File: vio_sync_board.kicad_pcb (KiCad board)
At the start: 2 copper layers, 50 x 57 mm, 12 parts, among them J1 Conn_IMU_Pi_Cam, Q1 BSS138, U1 MCP1700x-180xxTT

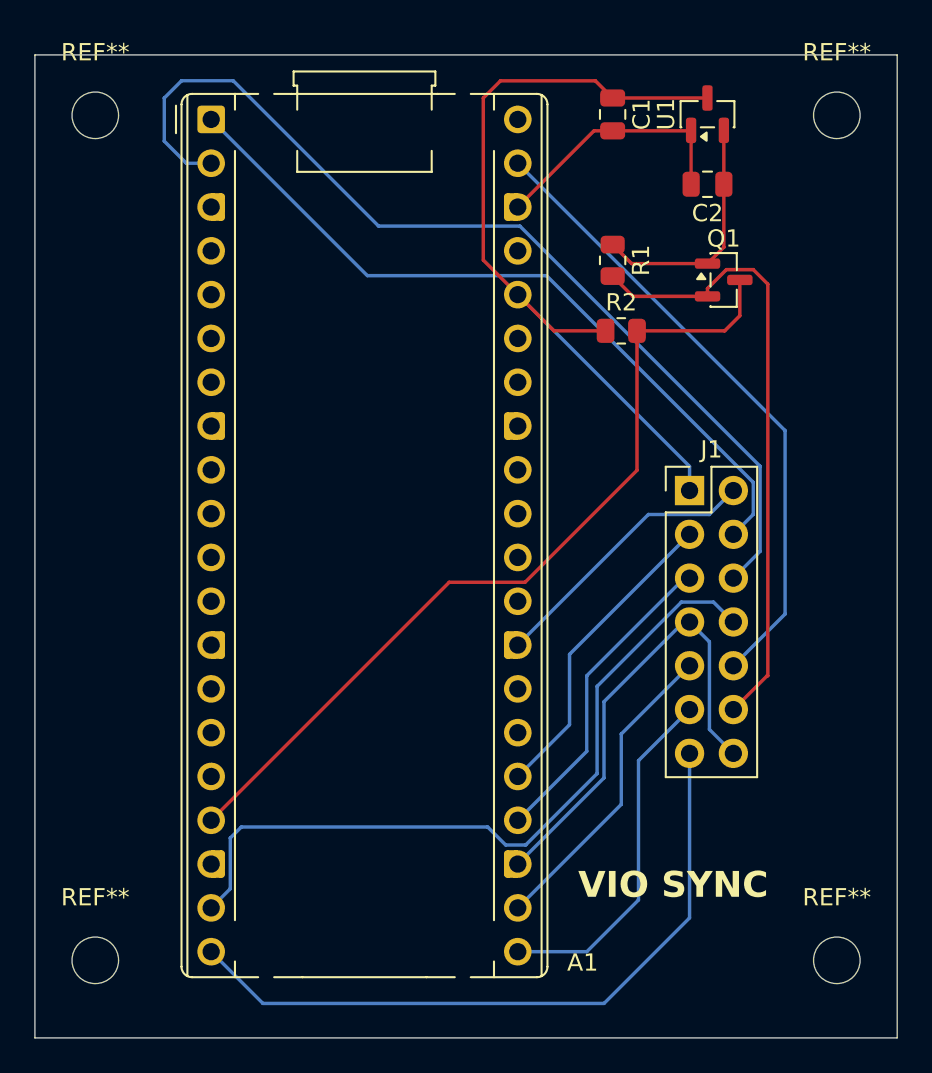
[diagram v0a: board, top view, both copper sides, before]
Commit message: refine header and hole position
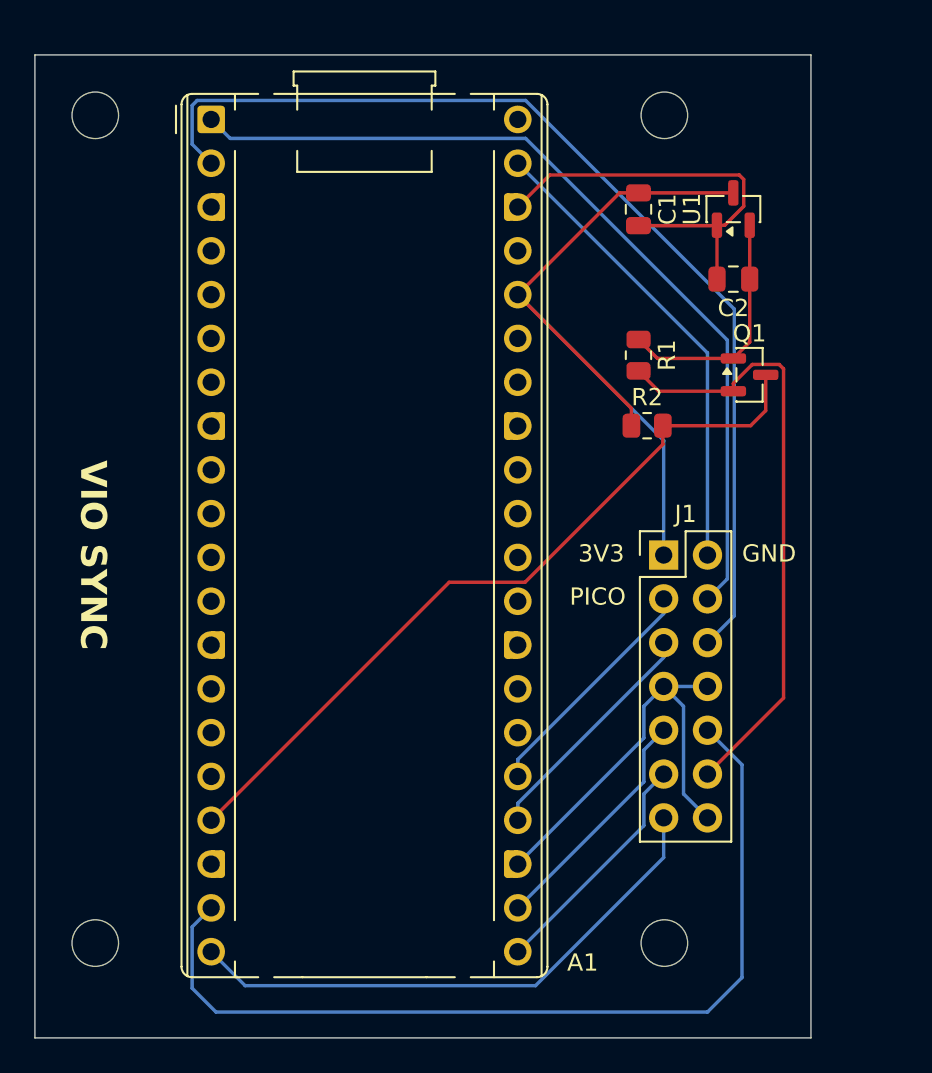
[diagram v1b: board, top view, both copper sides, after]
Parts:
- moved REF** 10.0 mm to (77.0, 98.0)
- moved REF** 10.0 mm to (77.0, 50.0)
- moved C1 5.70 mm to (75.5, 55.5)
- moved C2 5.70 mm to (81.0, 59.5)
- moved Q1 5.70 mm to (81.9, 65.0)
- moved R1 5.70 mm to (75.5, 63.9)
- moved R2 5.70 mm to (76.0, 68.0)
- moved U1 5.70 mm to (81.0, 55.4)
- moved J1 4.03 mm to (77.0, 75.5)
- moved REF** 1.00 mm to (44.0, 98.0)
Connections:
- J1 pad 10: /VSYS -> /TSYNC
- J1 pad 2: /GND -> /VSYS
- J1 pad 8: /TSYNC -> /GND
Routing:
- net /TSYNC: track 43.7 -> 53.6 mm
- net /VSYS: track 36.8 -> 27.3 mm
- net /IMU_INT: track 40.6 -> 32.4 mm
- net /GND: track 58.3 -> 50.2 mm
- net /UART0_TX: track 43.6 -> 50.7 mm
- net /SPI0_POCI: track 20.5 -> 13.8 mm
- net /SPI0_PICO: track 18.7 -> 13.8 mm
- net /XTR_3V3: track 49.6 -> 44.7 mm
- net /SPI0_SCK: track 18.3 -> 13.8 mm
- net /SPI0_CS: track 18.2 -> 13.8 mm
- net /3V3: track 47.5 -> 43.9 mm
- net /UART0_RX: track 57.1 -> 60.4 mm
- net /XTR_1V8: track 36.3 -> 35.2 mm
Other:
- board size 50 x 57 mm -> 45 x 57 mm
- board text added: "3V3"
- board text added: "GND"
- board text added: "PICO"

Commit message: track width
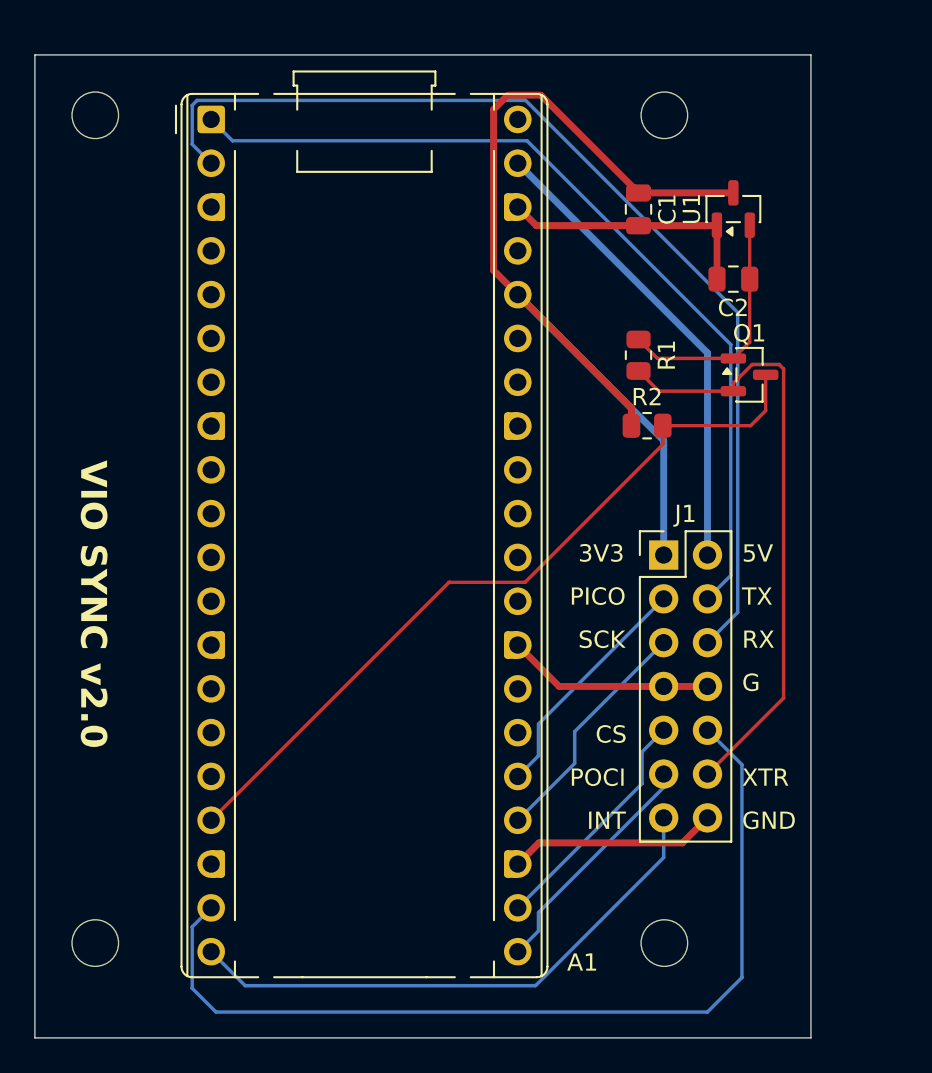
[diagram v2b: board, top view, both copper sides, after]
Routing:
- net /3V3: track 43.9 -> 56.8 mm
- net /GND: track 50.2 -> 39.2 mm
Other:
- board text added: "5V"
- board text added: "CS"
- board text added: "G"
- board text added: "INT"
- board text added: "POCI"
- board text added: "RX"
- board text added: "SCK"
- board text added: "TX"
- board text added: "VIO SYNC v2.0"
- board text added: "XTR"
- board text removed: "VIO SYNC"

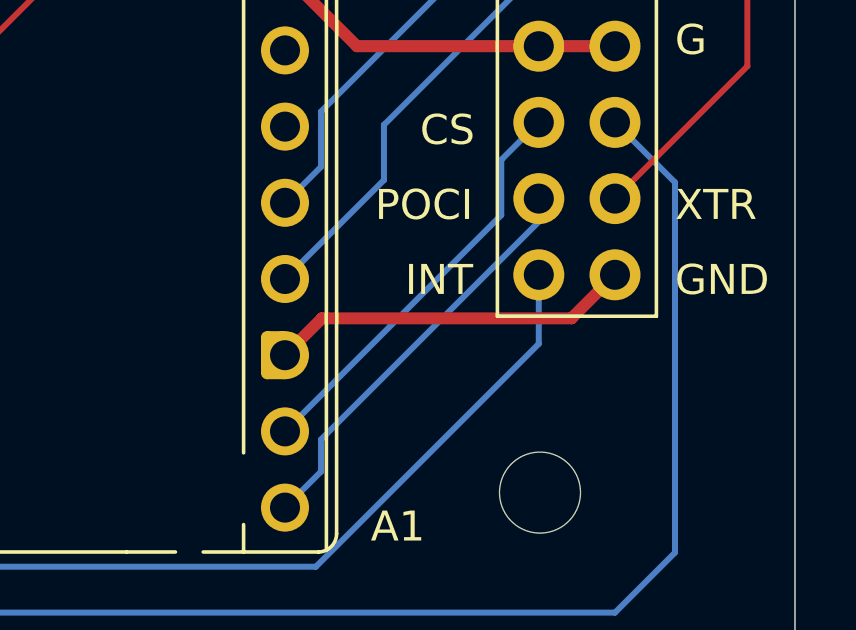
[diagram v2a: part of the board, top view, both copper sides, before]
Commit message: DNP pico & header
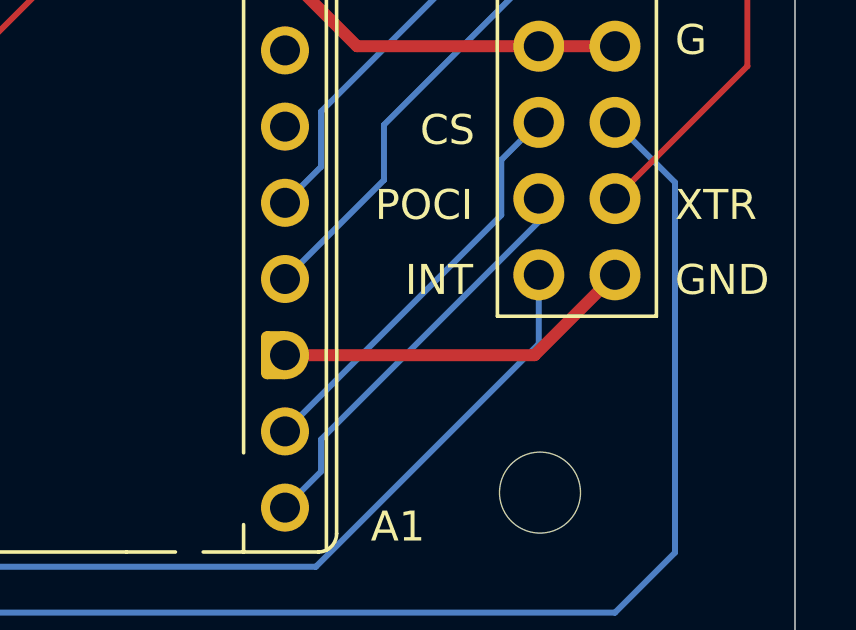
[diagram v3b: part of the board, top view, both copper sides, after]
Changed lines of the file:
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@@
 		(sheetname "/")
 		(sheetfile "vio_sync_board.kicad_sch")
-		(attr through_hole)
+		(attr through_hole exclude_from_bom dnp)
 		(fp_line
 			(start -1.38 -1.38)
@@
 		(sheetname "/")
 		(sheetfile "vio_sync_board.kicad_sch")
-		(attr through_hole)
+		(attr through_hole exclude_from_bom dnp)
 		(fp_line
 			(start -2.04 0.8)
@@
 	)
 	(segment
-		(start 78.049 92.191)
-		(end 69.729 92.191)
+		(start 76.82 93.42)
+		(end 68.5 93.42)
 		(width 0.4)
 		(layer "F.Cu")
@@
 	)
 	(segment
-		(start 75.5 56.4)
-		(end 69.58 56.4)
-		(width 0.4)
-		(layer "F.Cu")
-		(net 3)
-	)
-	(segment
-		(start 69.729 92.191)
-		(end 68.5 93.42)
+		(start 79.5 90.74)
+		(end 76.82 93.42)
 		(width 0.4)
 		(layer "F.Cu")
@@
 	)
 	(segment
-		(start 79.5 90.74)
-		(end 78.049 92.191)
+		(start 75.5 56.4)
+		(end 69.58 56.4)
 		(width 0.4)
 		(layer "F.Cu")
